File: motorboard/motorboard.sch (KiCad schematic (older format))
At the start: 1 part

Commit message: update test
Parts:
- U?: symbol MCU_Microchip_ATmega:ATmega328-AU -> motorboard-rescue:ATmega328-AU-MCU_Microchip_ATmega
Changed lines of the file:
@@
 $EndDescr
 $Comp
-L MCU_Microchip_ATmega:ATmega328-AU U?
+L motorboard-rescue:ATmega328-AU-MCU_Microchip_ATmega U?
 U 1 1 5E32C8DF
-P 5750 4050
-F 0 "U?" H 5550 5550 50  0000 C CNN
-F 1 "ATmega328-AU" H 6050 2400 50  0000 C CNN
-F 2 "Package_QFP:TQFP-32_7x7mm_P0.8mm" H 5750 4050 50  0001 C CIN
-F 3 "http://ww1.microchip.com/downloads/en/DeviceDoc/ATmega328_P%20AVR%20MCU%20with%20picoPower%20Technology%20Data%20Sheet%2040001984A.pdf" H 5750 4050 50  0001 C CNN
-	1    5750 4050
+P 5350 4050
+F 0 "U?" H 5150 5550 50  0000 C CNN
+F 1 "ATmega328-AU" H 5650 2400 50  0000 C CNN
+F 2 "Package_QFP:TQFP-32_7x7mm_P0.8mm" H 5350 4050 50  0001 C CIN
+F 3 "http://ww1.microchip.com/downloads/en/DeviceDoc/ATmega328_P%20AVR%20MCU%20with%20picoPower%20Technology%20Data%20Sheet%2040001984A.pdf" H 5350 4050 50  0001 C CNN
+	1    5350 4050
 	1    0    0    -1
 $EndComp

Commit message: Completed power things
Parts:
- removed U?: ATmega328-AU, Package_QFP:TQFP-32_7x7mm_P0.8mm, symbol motorboard-rescue:ATmega328-AU-MCU_Microchip_ATmega
- added C?: 0u1, Capacitor_SMD:C_0603_1608Metric, symbol Device:C_Small
- added J1: USB_B, Connector_USB:USB_B_OST_USB-B1HSxx_Horizontal, symbol Connector:USB_B
- added R2: 22k, Resistor_SMD:R_0603_1608Metric, symbol Device:R
- added R3: 43k, Resistor_SMD:R_0603_1608Metric, symbol Device:R
- added U1: CP2102N-A01-GQFN24, Package_DFN_QFN:QFN-24-1EP_4x4mm_P0.5mm_EP2.6x2.6mm_ThermalVias, symbol Interface_USB:CP2102N-A01-GQFN24
- added U?: ATmega328P-AU, Package_QFP:TQFP-32_7x7mm_P0.8mm, symbol MCU_Microchip_ATmega:ATmega328P-AU
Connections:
- net labels added: +3V3, DTR, GND, MISO, MOSI, RTS, RX, SCK, TX, VBUS
- wire segments 0 -> 38
- no-connect marks 0 -> 11
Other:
- note added: "USB to UART"

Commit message: Arduino is set up
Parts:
- added C?: 0u1, Capacitor_SMD:C_0603_1608Metric, symbol Device:C_Small
- added R?: R_Small, symbol Device:R_Small
- added SW?: SW_Push, symbol Switch:SW_Push
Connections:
- net +3V3: now also R?.1
- net DTR: now also C?.1
- net GND: now also SW?.1
- net at U?.29 (~RESET~/PC6): now also C?.2, R?.2, SW?.2
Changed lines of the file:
@@
 Text GLabel 7850 3800 2    50   Input ~ 0
 DTR
+Wire Wire Line
+	7850 3800 7500 3800
+$Comp
+L Device:C_Small C?
+U 1 1 5E3C31D9
+P 7400 3800
+F 0 "C?" H 7492 3846 50  0000 L CNN
+F 1 "0u1" V 7300 3850 50  0000 L CNN
+F 2 "Capacitor_SMD:C_0603_1608Metric" H 7400 3800 50  0001 C CNN
+F 3 "~" H 7400 3800 50  0001 C CNN
+	1    7400 3800
+	0    1    1    0
+$EndComp
+$Comp
+L Device:R_Small R?
+U 1 1 5E3C40B0
+P 7200 3500
+F 0 "R?" H 7259 3546 50  0000 L CNN
+F 1 "R_Small" H 6800 3550 50  0000 L CNN
+F 2 "" H 7200 3500 50  0001 C CNN
+F 3 "~" H 7200 3500 50  0001 C CNN
+	1    7200 3500
+	1    0    0    -1
+$EndComp
+Wire Wire Line
+	6350 3800 7200 3800
+Wire Wire Line
+	7300 3800 7200 3800
+Connection ~ 7200 3800
+$Comp
+L power:+3V3 #PWR?
+U 1 1 5E3C5E77
+P 7200 3400
+F 0 "#PWR?" H 7200 3250 50  0001 C CNN
+F 1 "+3V3" H 7215 3573 50  0000 C CNN
+F 2 "" H 7200 3400 50  0001 C CNN
+F 3 "" H 7200 3400 50  0001 C CNN
+	1    7200 3400
+	1    0    0    -1
+$EndComp
+$Comp
+L Switch:SW_Push SW?
+U 1 1 5E3C6E00
+P 7200 4150
+F 0 "SW?" V 7246 4102 50  0000 R CNN
+F 1 "SW_Push" V 7300 4550 50  0000 R CNN
+F 2 "" H 7200 4350 50  0001 C CNN
+F 3 "~" H 7200 4350 50  0001 C CNN
+	1    7200 4150
+	0    -1   -1   0
+$EndComp
+Wire Wire Line
+	7200 3950 7200 3800
+$Comp
+L power:GND #PWR?
+U 1 1 5E3C901A
+P 7200 4350
+F 0 "#PWR?" H 7200 4100 50  0001 C CNN
+F 1 "GND" H 7205 4177 50  0000 C CNN
+F 2 "" H 7200 4350 50  0001 C CNN
+F 3 "" H 7200 4350 50  0001 C CNN
+	1    7200 4350
+	1    0    0    -1
+$EndComp
+Wire Wire Line
+	7200 3600 7200 3800
 $EndSCHEMATC

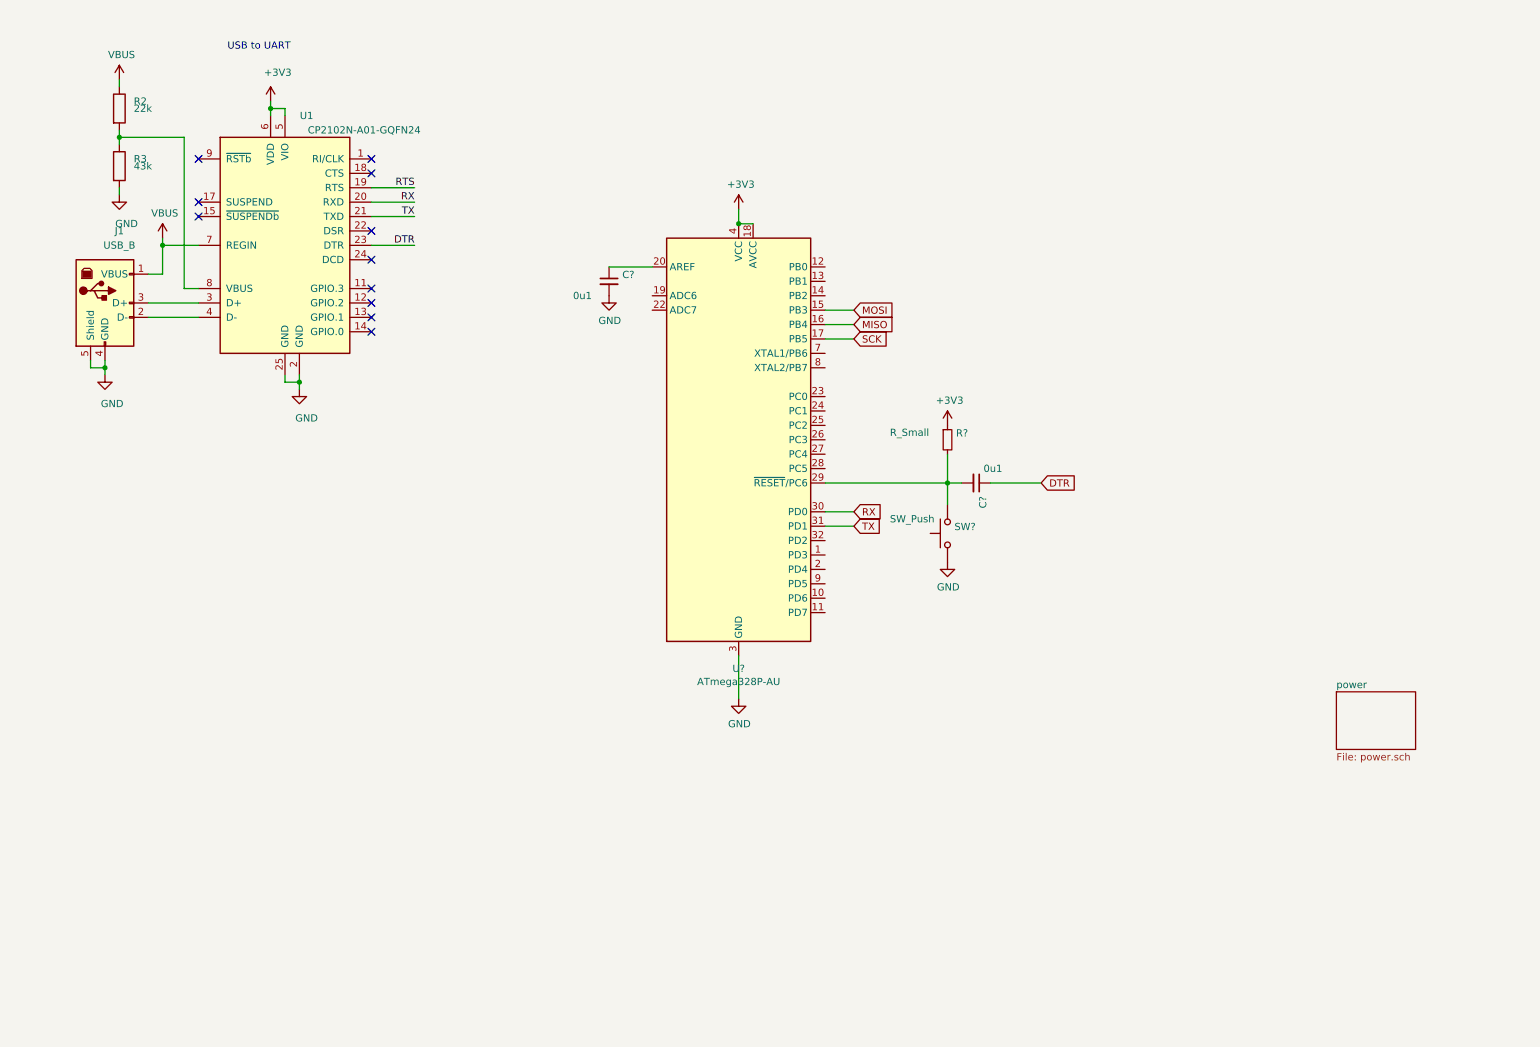
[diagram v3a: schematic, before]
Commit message: h bridge started
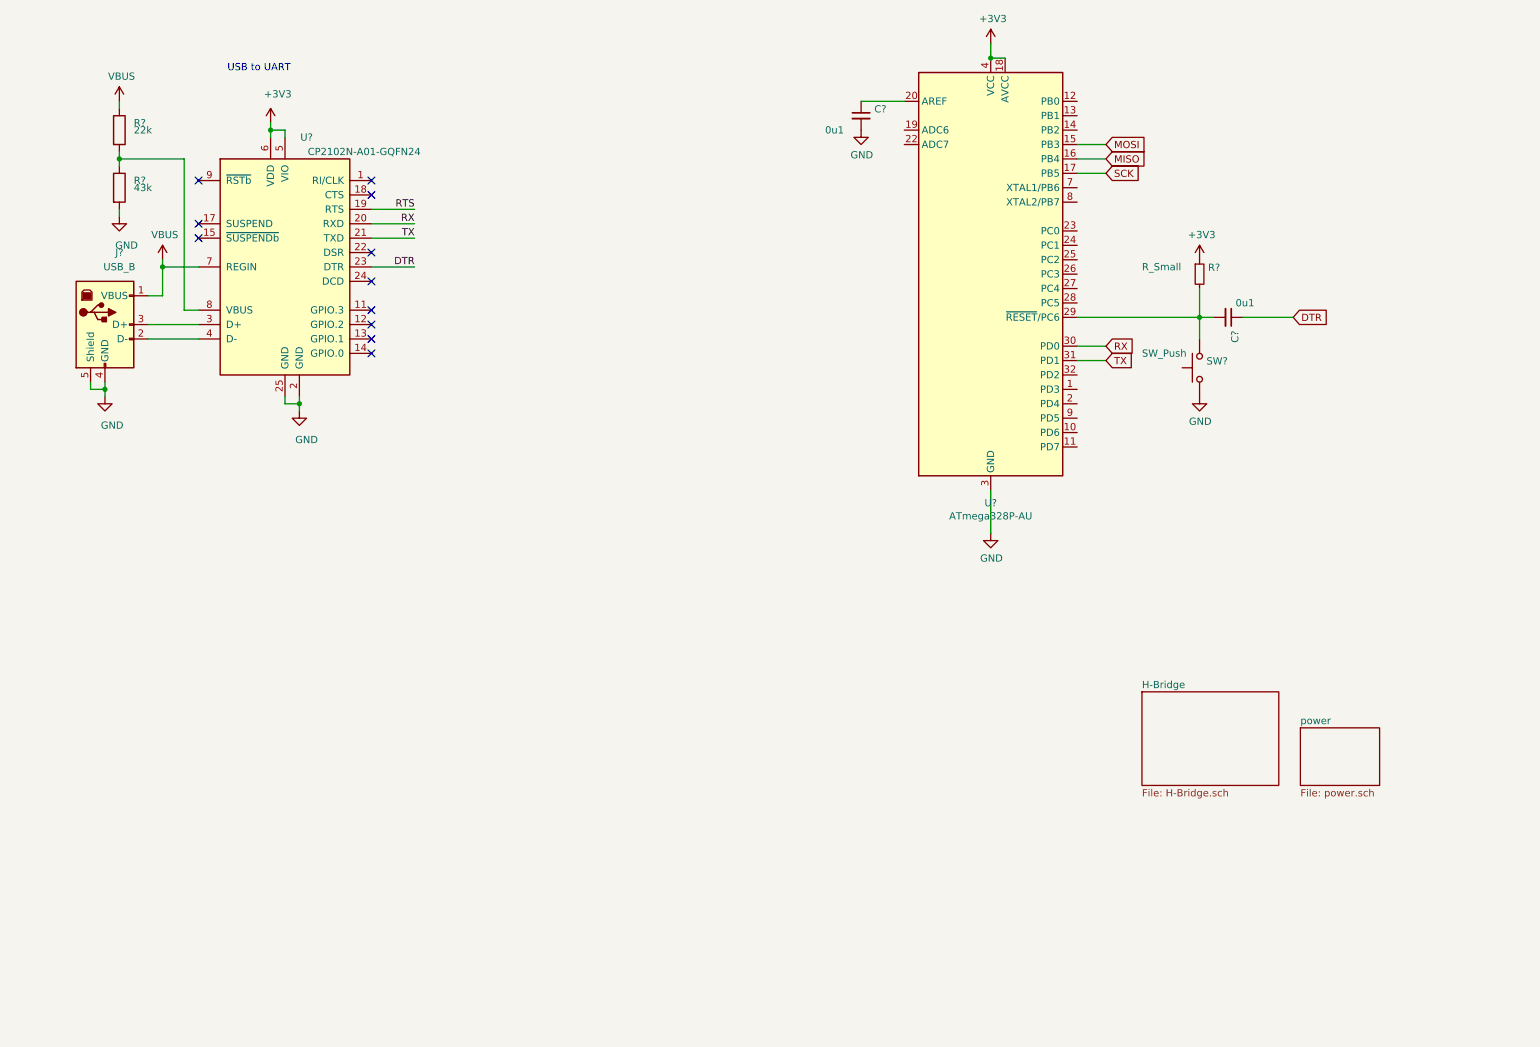
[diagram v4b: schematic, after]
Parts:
- removed J1: USB_B, Connector_USB:USB_B_OST_USB-B1HSxx_Horizontal, symbol Connector:USB_B
- removed R2: 22k, Resistor_SMD:R_0603_1608Metric, symbol Device:R
- removed R3: 43k, Resistor_SMD:R_0603_1608Metric, symbol Device:R
- removed U1: CP2102N-A01-GQFN24, Package_DFN_QFN:QFN-24-1EP_4x4mm_P0.5mm_EP2.6x2.6mm_ThermalVias, symbol Interface_USB:CP2102N-A01-GQFN24
- added J?: USB_B, Connector_USB:USB_B_OST_USB-B1HSxx_Horizontal, symbol Connector:USB_B
- added R?: 22k, Resistor_SMD:R_0603_1608Metric, symbol Device:R
- added R?: 43k, Resistor_SMD:R_0603_1608Metric, symbol Device:R
- added U?: CP2102N-A01-GQFN24, Package_DFN_QFN:QFN-24-1EP_4x4mm_P0.5mm_EP2.6x2.6mm_ThermalVias, symbol Interface_USB:CP2102N-A01-GQFN24
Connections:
- net +3V3: now also U?.5 (VIO), U?.6 (VDD)
- net DTR: now also U?.23 (DTR)
- net GND: now also J?.4 (GND), J?.5 (Shield), R?.2, U?.2 (GND), U?.25 (GND)
- net RTS: now also U?.19 (RTS)
- net RX: now also U?.20 (RXD)
- net TX: now also U?.21 (TXD)
- net VBUS: now also J?.1 (VBUS), R?.1, U?.7 (REGIN)
- new net: J?.2 (D-), U?.4 (D-)
- new net: J?.3 (D+), U?.3 (D+)
- new net: R?.1, R?.2, U?.8 (VBUS)
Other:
- moved on the sheet: C?, R?, SW?, U?

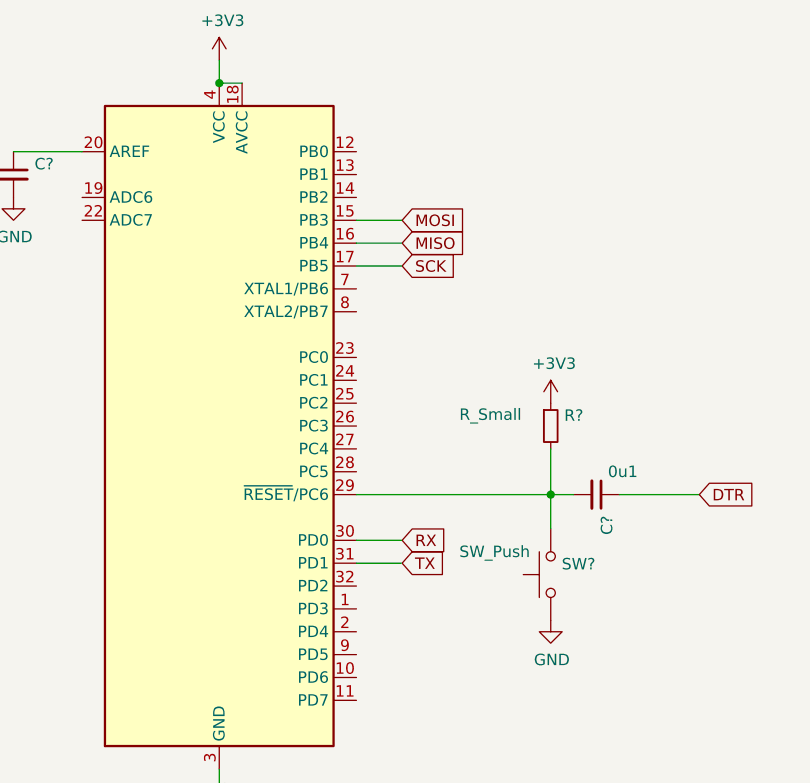
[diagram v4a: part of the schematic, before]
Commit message: basic h bridge complete
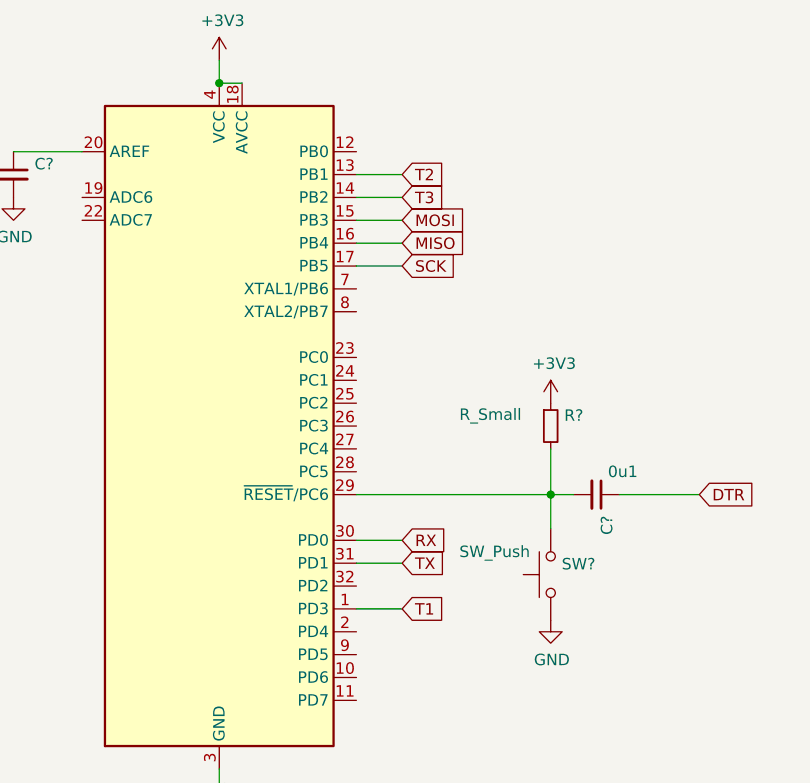
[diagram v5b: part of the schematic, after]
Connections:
- net T1: now reaches U?.1 (PD3)
- net T2: now reaches U?.13 (PB1)
- net T3: now reaches U?.14 (PB2)
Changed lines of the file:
@@
 F1 "H-Bridge.sch" 50
 $EndSheet
+Wire Wire Line
+	8100 3150 8300 3150
+Text GLabel 8300 3150 2    50   Input ~ 0
+T1
+Wire Wire Line
+	8100 1250 8300 1250
+Wire Wire Line
+	8100 1350 8300 1350
+Text GLabel 8300 1250 2    50   Input ~ 0
+T2
+Text GLabel 8300 1350 2    50   Input ~ 0
+T3
 $EndSCHEMATC

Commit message: Switched to TB6612
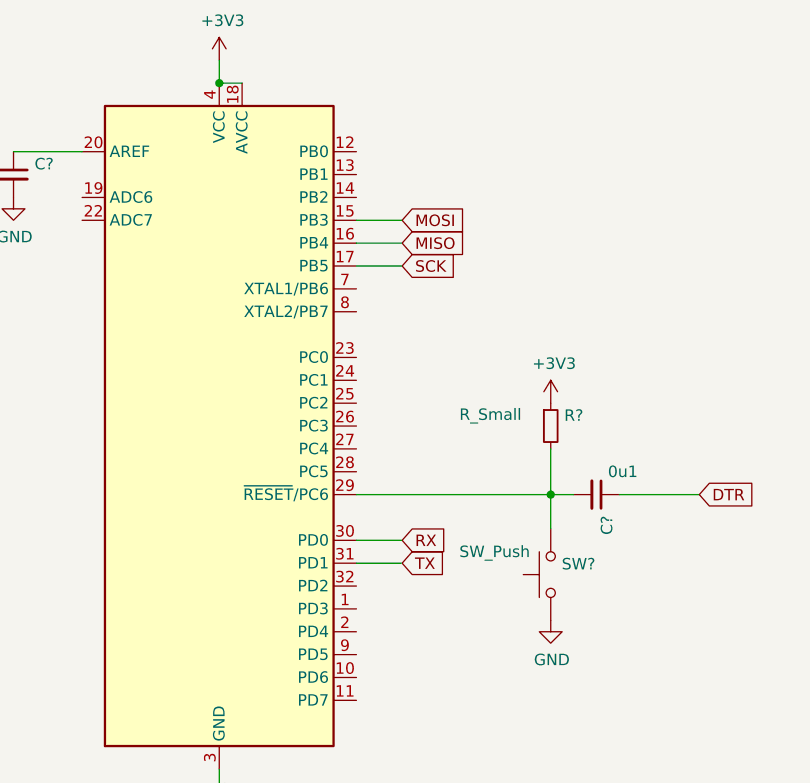
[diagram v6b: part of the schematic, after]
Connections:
- net T1: no longer names the net of U?.1 (PD3)
- net T2: no longer names the net of U?.13 (PB1)
- net T3: no longer names the net of U?.14 (PB2)
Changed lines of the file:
@@
 $EndSheet
-$Comp
-L MCU_Microchip_ATmega:ATmega328P-AU U?
-U 1 1 5E39C3D6
-P 7500 2350
-F 0 "U?" H 7500 761 50  0000 C CNN
-F 1 "ATmega328P-AU" H 7500 670 50  0000 C CNN
-F 2 "Package_QFP:TQFP-32_7x7mm_P0.8mm" H 7500 2350 50  0001 C CIN
-F 3 "http://ww1.microchip.com/downloads/en/DeviceDoc/ATmega328_P%20AVR%20MCU%20with%20picoPower%20Technology%20Data%20Sheet%2040001984A.pdf" H 7500 2350 50  0001 C CNN
-	1    7500 2350
-	1    0    0    -1
-$EndComp
 $Comp
 L power:+3V3 #PWR?
@@
 Wire Wire Line
 	7600 850  7500 850
-Connection ~ 7500 850
 $Comp
 L power:GND #PWR?
@@
 F1 "H-Bridge.sch" 50
 $EndSheet
-Wire Wire Line
-	8100 3150 8300 3150
-Text GLabel 8300 3150 2    50   Input ~ 0
-T1
-Wire Wire Line
-	8100 1250 8300 1250
-Wire Wire Line
-	8100 1350 8300 1350
-Text GLabel 8300 1250 2    50   Input ~ 0
-T2
-Text GLabel 8300 1350 2    50   Input ~ 0
-T3
+Connection ~ 7500 850
+$Comp
+L MCU_Microchip_ATmega:ATmega328P-AU U?
+U 1 1 5E39C3D6
+P 7500 2350
+F 0 "U?" H 7500 761 50  0000 C CNN
+F 1 "ATmega328P-AU" H 7500 670 50  0000 C CNN
+F 2 "Package_QFP:TQFP-32_7x7mm_P0.8mm" H 7500 2350 50  0001 C CIN
+F 3 "http://ww1.microchip.com/downloads/en/DeviceDoc/ATmega328_P%20AVR%20MCU%20with%20picoPower%20Technology%20Data%20Sheet%2040001984A.pdf" H 7500 2350 50  0001 C CNN
+	1    7500 2350
+	1    0    0    -1
+$EndComp
 $EndSCHEMATC
